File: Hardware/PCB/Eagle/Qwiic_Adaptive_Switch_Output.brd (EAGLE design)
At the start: 43.2 x 38.1 mm, 59 parts, among them J1 QWIIC_RIGHT_ANGLE, J4 QWIIC_RIGHT_ANGLE, SW1 CUI_SJ1-3513, SW2 CUI_SJ1-3513, U1 TCA9534

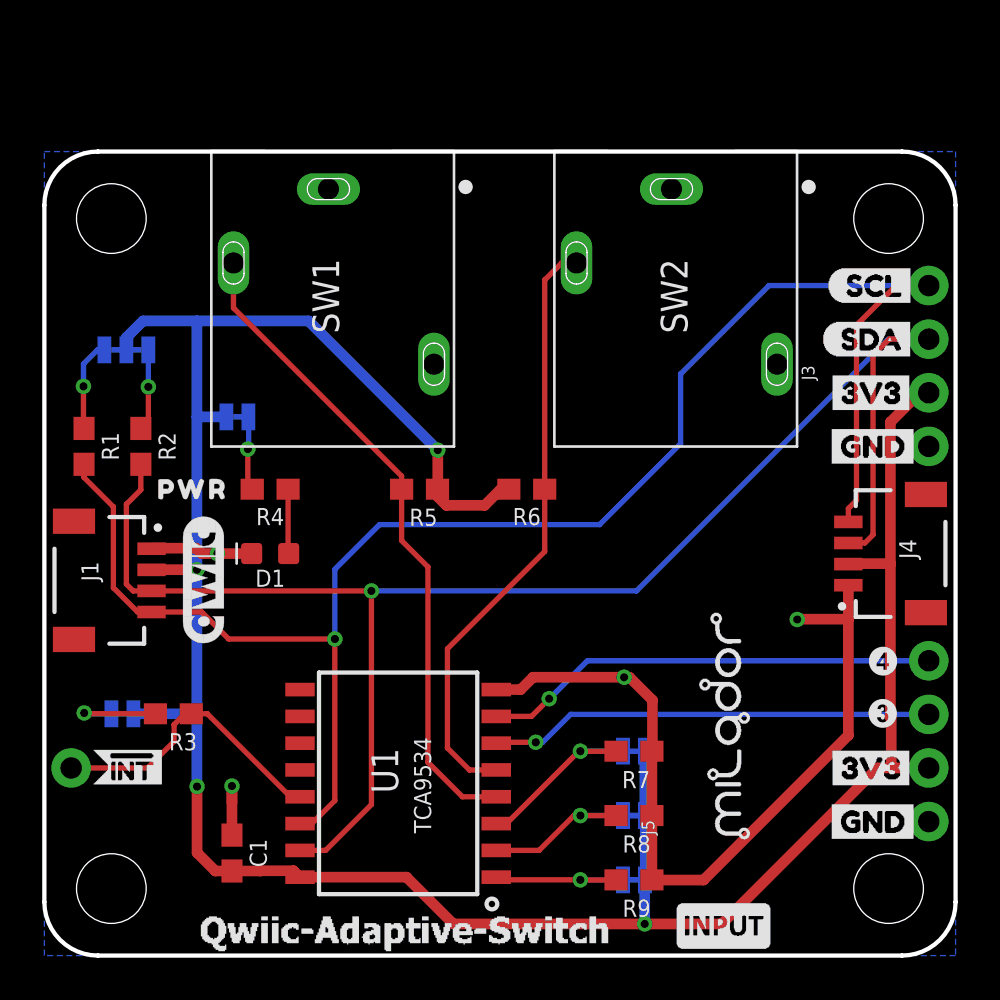
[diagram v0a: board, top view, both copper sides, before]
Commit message: Added Switch Output
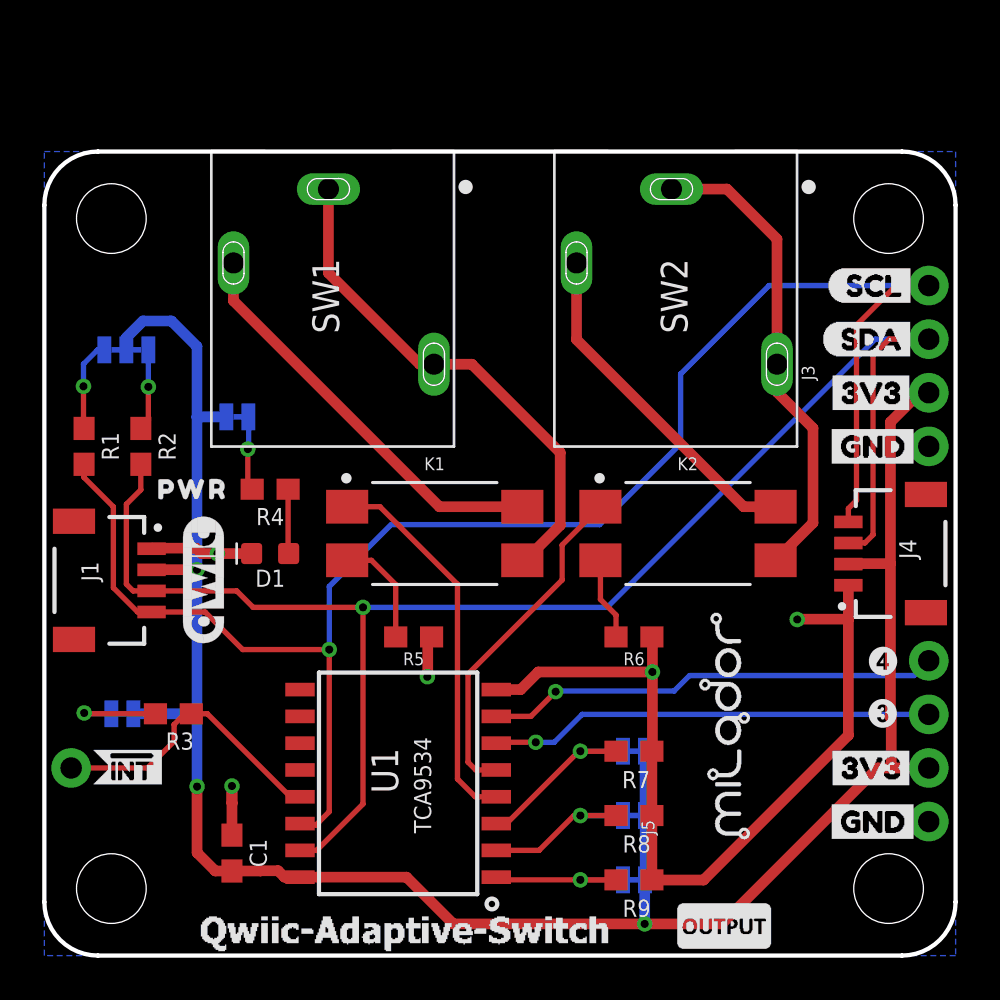
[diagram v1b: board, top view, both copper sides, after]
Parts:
- added K1, K2: G3VM-41DY1, milador_SMD:G3VM-41DY1
- LABEL_13: value (none) -> MILADOR-LOGO-; device milador:MILADOR_QWIIC_SWITCH -> milador:MILADOR_LOGO1
- LABEL_14: value MILADOR-LOGO- -> (none); device milador:MILADOR_LOGO1 -> output:#ADR2#0
- LABEL_15: device output:#ADR2#0 -> output:#ADR1#0
- LABEL_16: device output:#ADR1#0 -> output:#ADR0#0
- LABEL_17: device output:#ADR0#0 -> milador:MILADOR_QWIIC_SWITCH
- LABEL_18, LABEL_9: value MILADOR-SWITCH-NAME-SW-INPUT -> MILADOR-SWITCH-NAME-SW-OUTPUT; device milador:SWITCH-INPUT -> milador:SWITCH-OUTPUT
- R5: value 4.7k -> 220
- R6: value 4.7K -> 220
- moved LABEL_13 19.1 mm to (33.4, 11.0), turned to 90 degrees
- moved LABEL_17 17.1 mm to (17.1, 1.00), flipped to the top
- moved R6 8.65 mm to (27.9, 15.1), turned to 0 degrees
- moved R5 7.00 mm to (17.5, 15.1)
- moved LABEL_16 3.05 mm to (34.0, 3.59)
- moved LABEL_15 3.05 mm to (34.0, 6.64)
- moved LABEL_14 1.46 mm to (34.0, 9.68), flipped to the bottom, turned to 0 degrees
- renumbered LABEL_28 to U$28
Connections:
- new net N$4: K1.4, SW1.2
- new net N$5: K1.2, R5.1
- new net N$6: K1.3, SW1.1, SW1.3
- new net N$7: K2.2, R6.1
- new net N$8: K2.4, SW2.2
- new net N$9: K2.3, SW2.1, SW2.3
- net 3.3V: no longer R5.2, R6.2
- net GND: now also R5.2, R6.2; no longer SW1.1, SW1.3, SW2.1, SW2.3
- net P0: now also K1.1; no longer R5.1, SW1.2
- net P1: now also K2.1; no longer R6.1, SW2.2
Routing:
- net N$6: track 0.00 -> 24.4 mm
- net N$9: track 0.00 -> 22.6 mm
- net 3.3V: track 124.3 -> 103.6 mm, vias 4 -> 3
- net N$4: track 0.00 -> 19.5 mm
- net N$8: track 0.00 -> 16.3 mm
- net P0: track 31.4 -> 18.2 mm
- net P1: track 28.7 -> 16.2 mm
- net N$5: track 0.00 -> 5.26 mm
- net GND: track 46.3 -> 51.0 mm, vias 4 -> 5
- net N$7: track 0.00 -> 3.94 mm
- net SDA: track 76.3 -> 75.7 mm

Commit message: Updated PCB Designs to match input with output designs
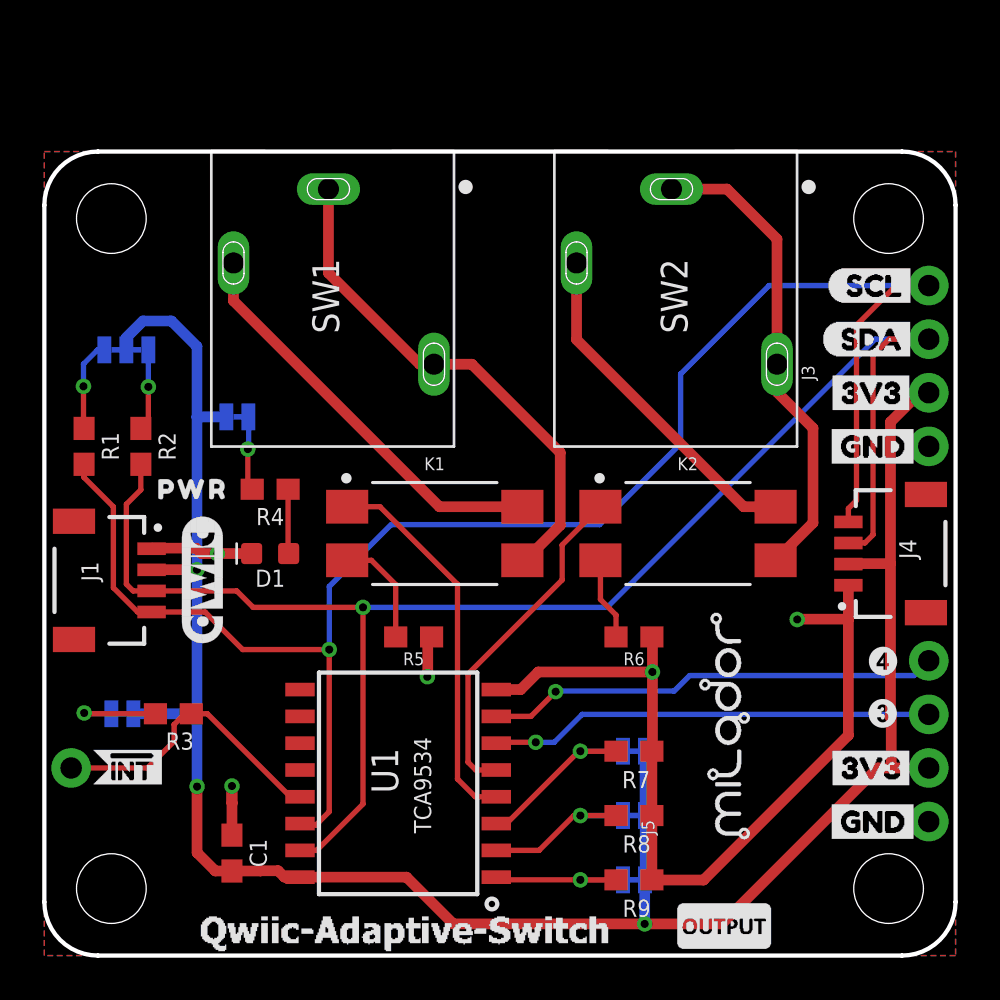
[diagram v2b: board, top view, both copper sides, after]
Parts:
- moved LABEL_6 0.05 mm to (7.50, 17.8)
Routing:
- added copper zone on layer 1, net GND
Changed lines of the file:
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@@
 <drawing>
 <settings>
-<setting alwaysvectorfont="yes"/>
+<setting alwaysvectorfont="no"/>
 <setting keepoldvectorfont="yes"/>
 <setting verticaltext="up"/>
 </settings>
-<grid distance="1.2" unitdist="mil" unit="mm" style="lines" multiple="1" display="yes" altdistance="0.005" altunitdist="inch" altunit="inch"/>
+<grid distance="0.127" unitdist="mm" unit="mm" style="lines" multiple="1" display="yes" altdistance="0.005" altunitdist="inch" altunit="inch"/>
 <layers>
 <layer number="1" name="Top" color="4" fill="1" visible="yes" active="yes"/>
@@
 </layers>
 <board>
-<fusionsync huburn="a.cGVyc29uYWw6dWUyYWQxOTI2" projecturn="a.cGVyc29uYWw6dWUyYWQxOTI2IzIwMjEwMTA3MzY5MTI4NTU2" f3durn="urn:adsk.wipprod:dm.lineage:MK9wFpCIT52xq48UYreXzw" pcbguid="" lastpulledtime="" lastsyncedchangeguid="" latestrevisionid="4595b786-bbd8-4743-b8d1-d3fe5783cdca" lastsyncedrevisionid="4595b786-bbd8-4743-b8d1-d3fe5783cdca" lastboardhashguid="cd902842-adca-e021-b2ff-fd426464cc86" lastpushedtime="2021-09-07T02:41:34Z" linktopcb3d="true"/>
+<fusionsync huburn="a.cGVyc29uYWw6dWUyYWQxOTI2" projecturn="a.cGVyc29uYWw6dWUyYWQxOTI2IzIwMjEwMTA3MzY5MTI4NTU2" f3durn="urn:adsk.wipprod:dm.lineage:MK9wFpCIT52xq48UYreXzw" pcbguid="" lastpulledtime="" lastsyncedchangeguid="" latestrevisionid="fe22f940-18ad-4771-afcc-ffbca6fb5588" lastsyncedrevisionid="fe22f940-18ad-4771-afcc-ffbca6fb5588" lastboardhashguid="979c33e1-b53c-9795-8501-e38620a062a6" lastpushedtime="2021-09-07T05:06:29Z" linktopcb3d="true"/>
 <plain>
 <wire x1="2.54" y1="38.1" x2="40.64" y2="38.1" width="0.2032" layer="20"/>
@@
 <element name="LABEL_19" library="buzzard_labels (44)" package="SCL6" value="" x="37.084" y="31.75" smashed="yes"/>
 <element name="LABEL_20" library="buzzard_labels (44)" package="SDA5" value="" x="36.83" y="29.21" smashed="yes"/>
-<element name="LABEL_6" library="SparkFun-Aesthetics" package="QWIIC_6MM" value="" x="7.5504" y="17.840959375" smashed="yes" rot="R90"/>
+<element name="LABEL_6" library="SparkFun-Aesthetics" package="QWIIC_6MM" value="" x="7.5" y="17.84" smashed="yes" rot="R90"/>
 <element name="LABEL_25" library="buzzard_labels (51)" package="SCL0" value="" x="41.656" y="31.75" smashed="yes" rot="MR0"/>
 <element name="LABEL_26" library="buzzard_labels (51)" package="SDA1" value="" x="41.529" y="29.21" smashed="yes" rot="MR0"/>
@@
 <wire x1="28.8163" y1="13.439040625" x2="28.8163" y2="15.0737" width="0.508" layer="1"/>
 <wire x1="28.8163" y1="15.0737" x2="28.79" y2="15.1" width="0.508" layer="1"/>
+<polygon width="0.2032" layer="1" isolate="0.3048">
+<vertex x="0" y="38.1"/>
+<vertex x="43.18" y="38.1"/>
+<vertex x="43.18" y="0"/>
+<vertex x="0" y="0"/>
+</polygon>
 </signal>
 <signal name="SCL_PU1">

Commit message: Updated PCB Mount holes
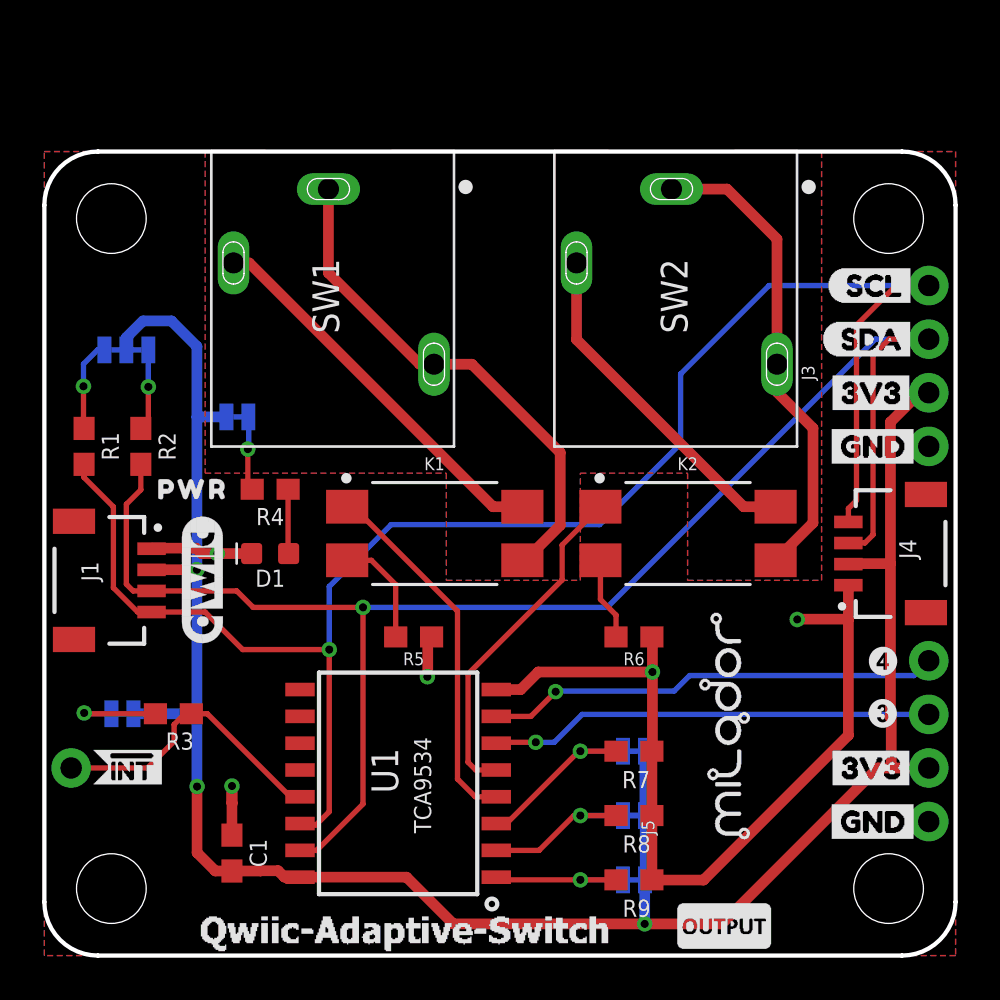
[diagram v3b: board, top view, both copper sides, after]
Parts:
- H1, H2: value STAND-OFF -> STAND-OFF-3.3; device SparkFun-Hardware:STAND-OFF -> milador:STAND-OFF-3.3
- JP3, JP4: value STAND-OFF -> STAND-OFF-3.3; device SparkFun:STAND-OFF -> milador:STAND-OFF-3.3
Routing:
- net N$4: track 19.5 -> 18.5 mm
- net P0: track 18.2 -> 17.4 mm
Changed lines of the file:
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@@
 <setting verticaltext="up"/>
 </settings>
-<grid distance="0.127" unitdist="mm" unit="mm" style="lines" multiple="1" display="yes" altdistance="0.005" altunitdist="inch" altunit="inch"/>
+<grid distance="0.025" unitdist="inch" unit="inch" style="lines" multiple="1" display="yes" altdistance="0.005" altunitdist="inch" altunit="inch"/>
 <layers>
 <layer number="1" name="Top" color="4" fill="1" visible="yes" active="yes"/>
@@
 </layers>
 <board>
-<fusionsync huburn="a.cGVyc29uYWw6dWUyYWQxOTI2" projecturn="a.cGVyc29uYWw6dWUyYWQxOTI2IzIwMjEwMTA3MzY5MTI4NTU2" f3durn="urn:adsk.wipprod:dm.lineage:MK9wFpCIT52xq48UYreXzw" pcbguid="" lastpulledtime="" lastsyncedchangeguid="" latestrevisionid="fe22f940-18ad-4771-afcc-ffbca6fb5588" lastsyncedrevisionid="fe22f940-18ad-4771-afcc-ffbca6fb5588" lastboardhashguid="979c33e1-b53c-9795-8501-e38620a062a6" lastpushedtime="2021-09-07T05:06:29Z" linktopcb3d="true"/>
+<fusionsync huburn="a.cGVyc29uYWw6dWUyYWQxOTI2" projecturn="a.cGVyc29uYWw6dWUyYWQxOTI2IzIwMjEwMTA3MzY5MTI4NTU2" f3durn="urn:adsk.wipprod:dm.lineage:MK9wFpCIT52xq48UYreXzw" pcbguid="" lastpulledtime="" lastsyncedchangeguid="" latestrevisionid="fa62e124-0746-4cbe-ad63-3b5afa9844e9" lastsyncedrevisionid="fa62e124-0746-4cbe-ad63-3b5afa9844e9" lastboardhashguid="d90a5bea-199f-b09b-55c8-c2be8575d095" lastpushedtime="2021-09-11T05:10:27Z" linktopcb3d="true"/>
 <plain>
 <wire x1="2.54" y1="38.1" x2="40.64" y2="38.1" width="0.2032" layer="20"/>
@@
 </autorouter>
 <elements>
-<element name="JP3" library="SparkFun" package="STAND-OFF" value="STAND-OFF" x="3.175" y="3.175" smashed="yes"/>
-<element name="JP4" library="SparkFun" package="STAND-OFF" value="STAND-OFF" x="40.005" y="3.175" smashed="yes"/>
+<element name="JP3" library="milador" library_urn="urn:adsk.eagle:library:12595918" package="STAND-OFF-3.3" package3d_urn="urn:adsk.eagle:package:30775189/1" value="STAND-OFF-3.3" x="3.175" y="3.175" smashed="yes"/>
+<element name="JP4" library="milador" library_urn="urn:adsk.eagle:library:12595918" package="STAND-OFF-3.3" package3d_urn="urn:adsk.eagle:package:30775189/1" value="STAND-OFF-3.3" x="40.005" y="3.175" smashed="yes"/>
 <element name="J1" library="milador_SMD" library_urn="urn:adsk.eagle:library:27847482" package="CONNECTORS_JST04_1MM_RA" package3d_urn="urn:adsk.eagle:package:29222212/3" value="QWIIC_RIGHT_ANGLE" x="5.08" y="17.78" smashed="yes" rot="R270">
 <attribute name="NAME" x="1.7526" y="18.669" size="0.8128" layer="21" font="vector" ratio="15" rot="R270"/>
@@
 <element name="U$28" library="buzzard_labels (44)" package="GND4" value="" x="41.656" y="24.13" smashed="yes" rot="MR0"/>
 <element name="LABEL_27" library="buzzard_labels (44)" package="3V33" value="" x="41.529" y="26.67" smashed="yes" rot="MR0"/>
-<element name="H1" library="SparkFun-Hardware" package="STAND-OFF" value="STAND-OFF" x="40.005" y="34.925" smashed="yes">
-<attribute name="VALUE" x="40.005" y="32.893" size="0.6096" layer="27" font="vector" ratio="20" align="top-center"/>
-</element>
-<element name="H2" library="SparkFun-Hardware" package="STAND-OFF" value="STAND-OFF" x="3.175" y="34.925" smashed="yes"/>
+<element name="H1" library="milador" library_urn="urn:adsk.eagle:library:12595918" package="STAND-OFF-3.3" package3d_urn="urn:adsk.eagle:package:30775189/1" value="STAND-OFF-3.3" x="40.005" y="34.925" smashed="yes"/>
+<element name="H2" library="milador" library_urn="urn:adsk.eagle:library:12595918" package="STAND-OFF-3.3" package3d_urn="urn:adsk.eagle:package:30775189/1" value="STAND-OFF-3.3" x="3.175" y="34.925" smashed="yes"/>
 <element name="R3" library="milador_SMD" library_urn="urn:adsk.eagle:library:27847482" package="0603" package3d_urn="urn:adsk.eagle:package:29222124/2" value="10k" x="6.11378125" y="11.4587" smashed="yes" rot="R180">
 <attribute name="NAME" x="6.41858125" y="10.5697" size="0.8128" layer="21" font="vector" ratio="15" rot="R180" align="bottom-center"/>
@@
 <polygon width="0.2032" layer="16" isolate="0.3048">
 <vertex x="0" y="38.1"/>
+<vertex x="7.62" y="38.1"/>
+<vertex x="7.62" y="22.86"/>
+<vertex x="19.05" y="22.86"/>
+<vertex x="19.05" y="17.78"/>
+<vertex x="25.4" y="17.78"/>
+<vertex x="25.4" y="22.86"/>
+<vertex x="30.48" y="22.86"/>
+<vertex x="30.48" y="17.78"/>
+<vertex x="36.83" y="17.78"/>
+<vertex x="36.83" y="38.1"/>
 <vertex x="43.18" y="38.1"/>
 <vertex x="43.18" y="0"/>
@@
 <polygon width="0.2032" layer="1" isolate="0.3048">
 <vertex x="0" y="38.1"/>
+<vertex x="7.62" y="38.1"/>
+<vertex x="7.62" y="22.86"/>
+<vertex x="19.05" y="22.86"/>
+<vertex x="19.05" y="17.78"/>
+<vertex x="25.4" y="17.78"/>
+<vertex x="25.4" y="22.86"/>
+<vertex x="30.48" y="22.86"/>
+<vertex x="30.48" y="17.78"/>
+<vertex x="36.83" y="17.78"/>
+<vertex x="36.83" y="38.1"/>
 <vertex x="43.18" y="38.1"/>
 <vertex x="43.18" y="0"/>
@@
 <contactref element="U1" pad="4"/>
 <wire x1="21.414" y1="7.525" x2="20.4216" y2="7.525" width="0.254" layer="1"/>
-<wire x1="19.576684375" y1="17.5971125" x2="19.576684375" y2="8.369915625" width="0.254" layer="1"/>
+<wire x1="19.576684375" y1="16.3271125" x2="19.576684375" y2="8.369915625" width="0.254" layer="1"/>
 <wire x1="20.4216" y1="7.525" x2="19.576684375" y2="8.369915625" width="0.254" layer="1"/>
 <contactref element="K1" pad="1"/>
-<wire x1="14.35" y1="21.27" x2="15.903796875" y2="21.27" width="0.254" layer="1"/>
-<wire x1="15.903796875" y1="21.27" x2="19.576684375" y2="17.5971125" width="0.254" layer="1"/>
+<wire x1="14.35" y1="21.27" x2="14.633796875" y2="21.27" width="0.254" layer="1"/>
+<wire x1="14.633796875" y1="21.27" x2="19.576684375" y2="16.3271125" width="0.254" layer="1"/>
 </signal>
 <signal name="P2">
@@
 <contactref element="SW1" pad="2"/>
 <contactref element="K1" pad="4"/>
-<wire x1="22.65" y1="21.27" x2="18.7197625" y2="21.27" width="0.508" layer="1"/>
-<wire x1="8.962" y1="31.0277625" x2="8.962" y2="32.822" width="0.508" layer="1"/>
-<wire x1="18.7197625" y1="21.27" x2="8.962" y2="31.0277625" width="0.508" layer="1"/>
+<wire x1="22.65" y1="21.27" x2="21.2597625" y2="21.27" width="0.508" layer="1"/>
+<wire x1="21.2597625" y1="21.27" x2="9.7077625" y2="32.822" width="0.508" layer="1"/>
+<wire x1="8.962" y1="32.822" x2="9.7077625" y2="32.822" width="0.508" layer="1"/>
 </signal>
 <signal name="N$6">

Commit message: Updated footprints to 0805 packages
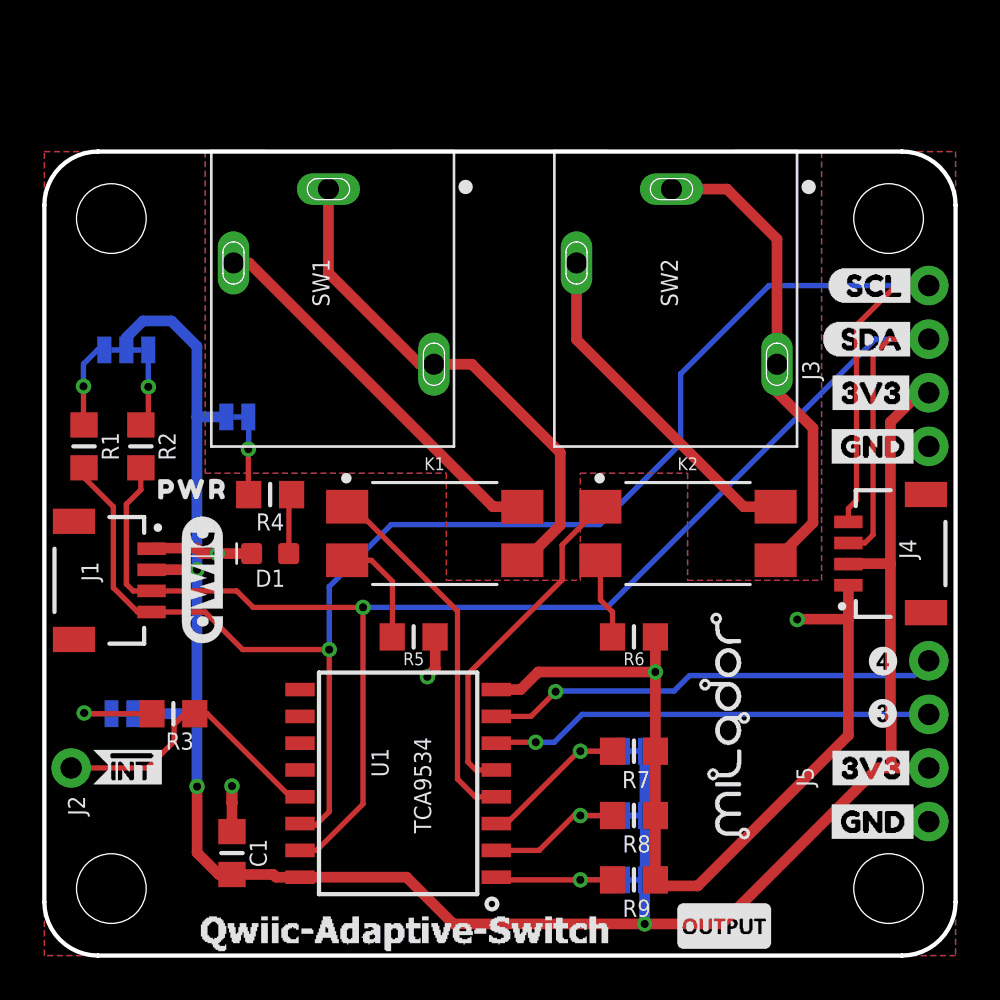
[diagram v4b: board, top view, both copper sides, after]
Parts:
- C1, R1, R2, R3, R4, R5, R6, R7, R8, R9: device milador_SMD:0603 -> milador_SMD:0805-MP
- moved R4 0.25 mm to (10.7, 21.8)
